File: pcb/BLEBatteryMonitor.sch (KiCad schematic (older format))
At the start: 20 parts, among them IC101 ATTINY3224-SS, K101 CONN_3, P101 CONN_1, P102 CONN_2, P103 CONN_2, P104 DEBUG, P105 CONN_1, U101 NCP1117ST50T3G, U102 INA219-module, U103 NCP718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

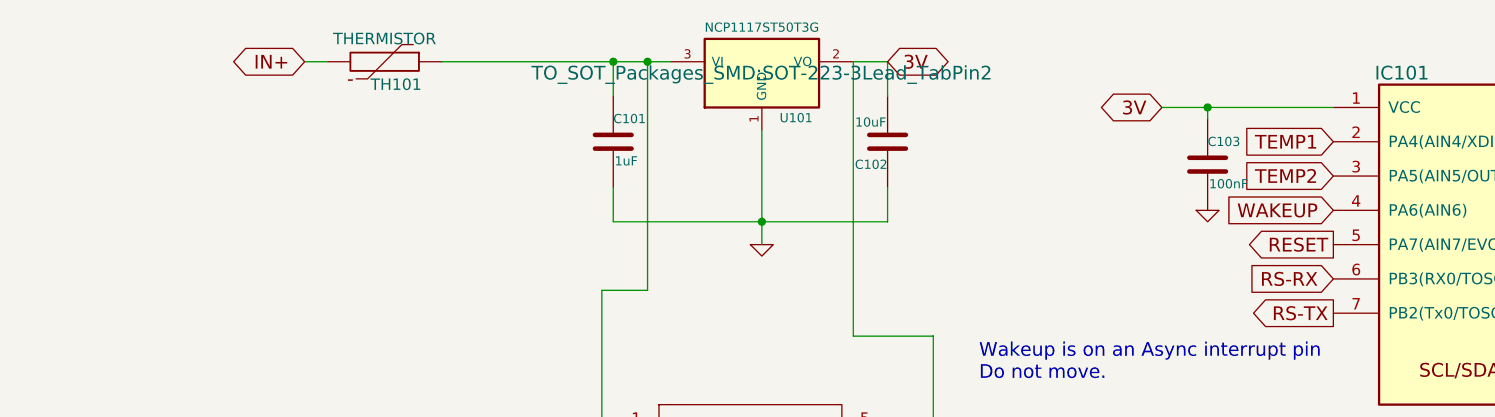
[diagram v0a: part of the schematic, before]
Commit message: Fixed 49day overflows
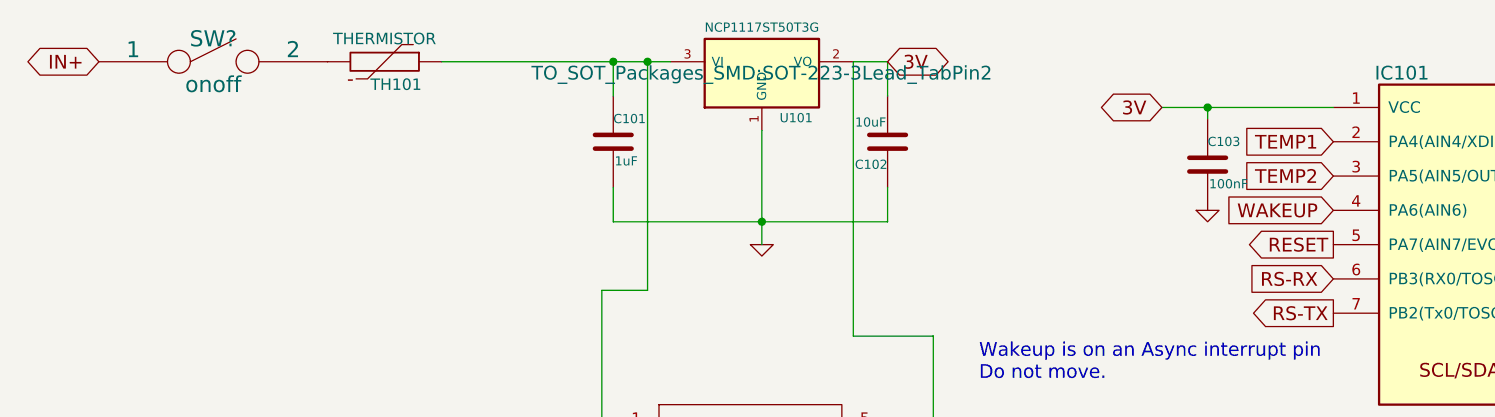
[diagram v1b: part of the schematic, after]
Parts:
- added SW?: onoff, symbol SPST
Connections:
- net IN+: now also SW?.1; no longer TH101.2
- new net: SW?.2, TH101.2
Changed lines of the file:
@@
 $EndComp
 Wire Wire Line
-	5450 1500 6200 1500
+	5450 1500 5650 1500
+Wire Wire Line
+	5650 1500 6200 1500
 Wire Wire Line
 	5650 1550 5650 1500
@@
 	4250 1850 4250 2000
 Wire Wire Line
-	4250 2000 3050 2000
+	4250 2000 3700 2000
+Wire Wire Line
+	3700 2000 3050 2000
 Wire Wire Line
 	3050 2000 3050 1850
 Wire Wire Line
-	3700 1600 3700 2100
+	3700 1600 3700 2000
+Wire Wire Line
+	3700 2000 3700 2100
 Connection ~ 3700 2000
 Wire Wire Line
-	2300 1300 3300 1300
+	2300 1300 3050 1300
+Wire Wire Line
+	3050 1300 3200 1300
+Wire Wire Line
+	3200 1300 3300 1300
 Wire Wire Line
 	3050 1300 3050 1450
@@
 Text GLabel 4250 1300 2    60   BiDi ~ 0
 3V
-Text GLabel 1700 1300 0    60   BiDi ~ 0
+Text GLabel 800  1300 0    60   BiDi ~ 0
 IN+
 Connection ~ 3050 1300
@@
 	0    1    1    0
 $EndComp
-Wire Wire Line
-	1700 1300 1800 1300
 $Comp
 L R R104
@@
 Text Notes 650  6200 0    60   ~ 0
 https://github.com/SpenceKonde/megaTinyCore/blob/e59fc3046dd69f951497506e8f441a6818c28be5/megaavr/extras/PowerSave.md\n\nLDL117 has 250uA Iq and has input of 20V https://www.st.com/resource/en/datasheet/ldl1117.pdf\n
+$Comp
+L SPST SW?
+U 1 1 6322D892
+P 1300 1300
+F 0 "SW?" H 1300 1400 70  0000 C CNN
+F 1 "onoff" H 1300 1200 70  0000 C CNN
+F 2 "" H 1300 1300 60  0000 C CNN
+F 3 "" H 1300 1300 60  0000 C CNN
+	1    1300 1300
+	1    0    0    -1
+$EndComp
 $EndSCHEMATC
